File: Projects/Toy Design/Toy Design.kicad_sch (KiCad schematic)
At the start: 42 parts, among them J1 Conn_01x01_Pin, J2 Conn_01x01_Pin, J3 FTSH-107-01-X-DV-K-TR, U1 TLV61048DBVR, U10 STM32G030K6T6, U11 MCP3208-CI/SL, U2 MCP73123, U3 NCP1117-5.0_SOT223, U4 MLX90333, U5 A1330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

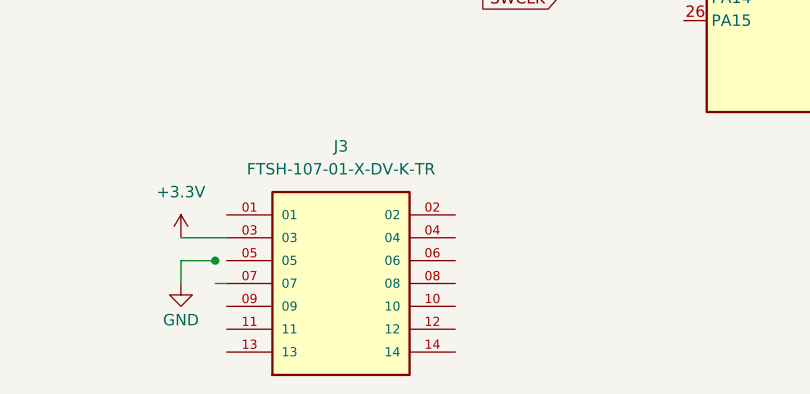
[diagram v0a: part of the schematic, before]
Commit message: Pushing connector connected to all signals
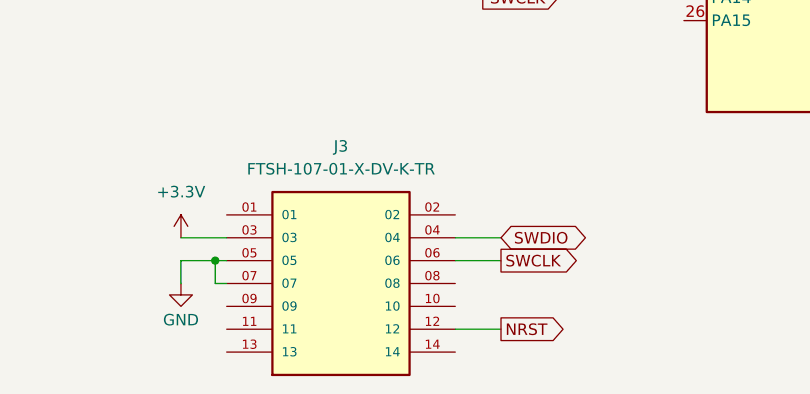
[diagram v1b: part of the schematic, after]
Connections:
- net GND: now also J3.05, J3.07
- net NRST: now also J3.12
- net SWCLK: now also J3.06
- net SWDIO: now also J3.04
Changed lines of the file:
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@@
+	)
+	(junction
+		(at 246.38 234.95)
+		(diameter 0)
+		(color 0 0 0 0)
 	)
 	(junction
@@
 	)
 	(junction
-		(at 246.38 234.95)
-		(diameter 0)
-		(color 0 0 0 0)
-	)
-	(junction
 		(at 167.64 49.53)
 		(diameter 0)
@@
 	(wire
 		(pts
+			(xy 246.38 234.95) (xy 247.65 234.95)
+		)
+		(stroke
+			(width 0)
+			(type default)
+		)
+	)
+	(wire
+		(pts
 			(xy 33.02 38.1) (xy 36.83 38.1)
 		)
@@
 	(wire
 		(pts
+			(xy 273.05 232.41) (xy 278.13 232.41)
+		)
+		(stroke
+			(width 0)
+			(type default)
+		)
+	)
+	(wire
+		(pts
 			(xy 153.67 115.57) (xy 153.67 125.73)
 		)
@@
 	(wire
 		(pts
+			(xy 273.05 234.95) (xy 278.13 234.95)
+		)
+		(stroke
+			(width 0)
+			(type default)
+		)
+	)
+	(wire
+		(pts
 			(xy 204.47 39.37) (xy 204.47 38.1)
 		)
@@
 	(wire
 		(pts
+			(xy 273.05 242.57) (xy 278.13 242.57)
+		)
+		(stroke
+			(width 0)
+			(type default)
+		)
+	)
+	(wire
+		(pts
 			(xy 71.12 181.61) (xy 76.2 181.61)
 		)
@@
 		(pts
 			(xy 60.96 53.34) (xy 59.69 53.34)
+		)
+		(stroke
+			(width 0)
+			(type default)
+		)
+	)
+	(wire
+		(pts
+			(xy 246.38 234.95) (xy 246.38 237.49)
 		)
 		(stroke
@@
 		)
 	)
+	(global_label "NRST"
+		(shape output)
+		(at 278.13 242.57 0)
+		(fields_autoplaced yes)
+		(effects
+			(font
+				(size 1.27 1.27)
+			)
+			(justify left)
+		)
+		(property "Intersheetrefs" "${INTERSHEET_REFS}"
+			(at 285.8928 242.57 0)
+			(hide yes)
+			(show_name no)
+			(do_not_autoplace no)
+			(effects
+				(font
+					(size 1.27 1.27)
+				)
+				(justify left)
+			)
+		)
+	)
 	(global_label "OUT_U6"
 		(shape output)
@@
 	)
 	(global_label "SWCLK"
+		(shape output)
+		(at 278.13 234.95 0)
+		(fields_autoplaced yes)
+		(effects
+			(font
+				(size 1.27 1.27)
+			)
+			(justify left)
+		)
+		(property "Intersheetrefs" "${INTERSHEET_REFS}"
+			(at 287.3442 234.95 0)
+			(hide yes)
+			(show_name no)
+			(do_not_autoplace no)
+			(effects
+				(font
+					(size 1.27 1.27)
+				)
+				(justify left)
+			)
+		)
+	)
+	(global_label "SWCLK"
 		(shape input)
 		(at 284.48 205.74 180)
@@
 			(hide yes)
 			(show_name no)
+			(do_not_autoplace no)
+			(effects
+				(font
+					(size 1.27 1.27)
+				)
+				(justify left)
+			)
+		)
+	)
+	(global_label "SWDIO"
+		(shape bidirectional)
+		(at 278.13 232.41 0)
+		(fields_autoplaced yes)
+		(effects
+			(font
+				(size 1.27 1.27)
+			)
+			(justify left)
+		)
+		(property "Intersheetrefs" "${INTERSHEET_REFS}"
+			(at 288.0927 232.41 0)
+			(hide yes)
+			(show_name no)
